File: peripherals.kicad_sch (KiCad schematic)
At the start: 14 parts, among them U5 FT230XQ

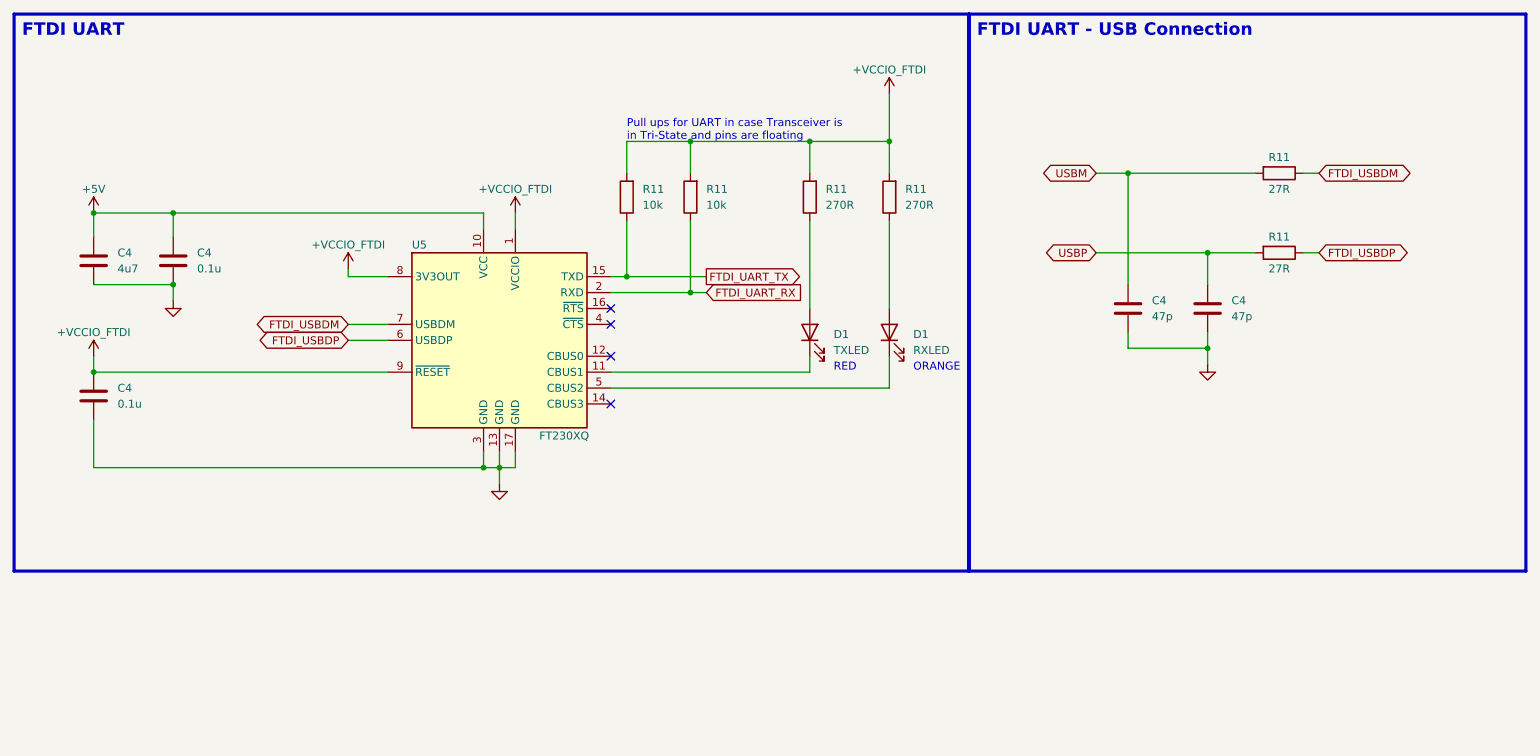
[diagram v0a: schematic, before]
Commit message: Added ESD, updated Footprints, BOM, etc.
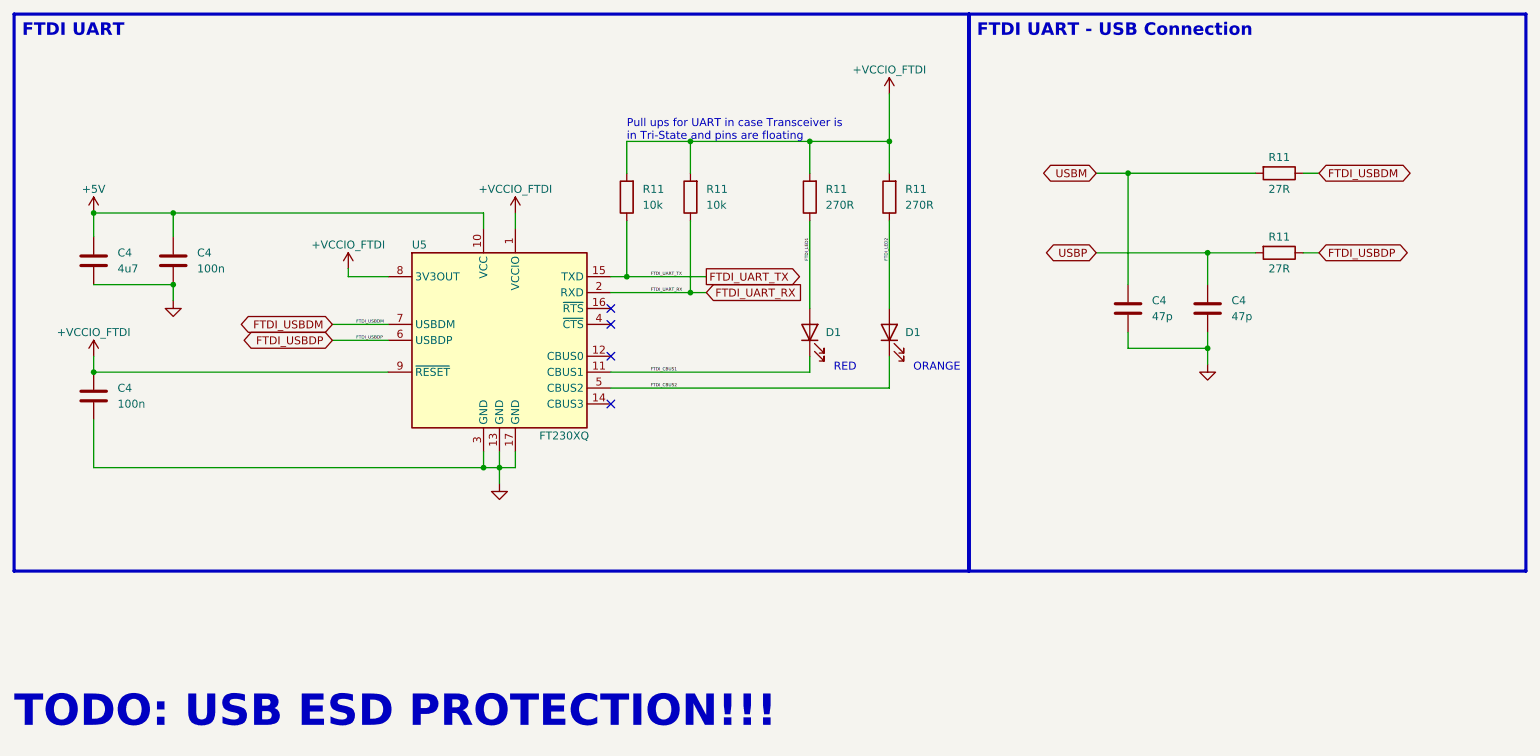
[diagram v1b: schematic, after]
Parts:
- C4: value 0.1u -> 100n
- D1: value TXLED -> SML-LX0402SIC-TR
- D1: value RXLED -> SML-LX0402SOC-TR; Feld4 SML-LX0402SOC-TR -> (none); MFN (none) -> SML-LX0402SOC-TR
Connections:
- net FTDI_CBUS1: now reaches D1.1 (K), U5.11 (CBUS1)
- net FTDI_CBUS2: now reaches D1.1 (K), U5.5 (CBUS2)
- net FTDI_LED2: now reaches D1.2 (A), R11.1
- net FTDI_LED1: now reaches D1.2 (A), R11.1
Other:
- note added: "TODO: USB ESD PROTECTION!!!"
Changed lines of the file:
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@@
     (stroke (width 0) (type default))
   )
-  (wire (pts (xy 78.74 77.47) (xy 85.09 77.47))
+  (wire (pts (xy 76.2 77.47) (xy 85.09 77.47))
     (stroke (width 0) (type default))
   )
@@
     (stroke (width 0) (type default))
   )
-  (wire (pts (xy 78.74 74.93) (xy 85.09 74.93))
+  (wire (pts (xy 76.2 74.93) (xy 85.09 74.93))
     (stroke (width 0) (type default))
   )
@@
     (effects (font (size 2 2) (thickness 0.254) bold (color 100 100 100 1)) (justify left bottom))
   )
+  (text "TODO: USB ESD PROTECTION!!!" (at 25.4 139.7 0)
+    (effects (font (size 5 5) (thickness 1) bold (color 150 0 0 1)) (justify left bottom))
+  )
   (text "Pull ups for UART in case Transceiver is\nin Tri-State and pins are floating"
     (at 123.19 45.72 0)
@@
     (effects (font (size 1.27 1.27)) (justify left bottom))
   )
-  (global_label "FTDI_USBDP" (shape bidirectional) (at 78.74 77.47 180) (fields_autoplaced)
+  (label "FTDI_UART_TX" (at 127 67.31 0) (fields_autoplaced)
+    (effects (font (size 0.5 0.5)) (justify left bottom))
+    (property "Netclass" "UART" (at 127 67.81 0)
+      (effects (font (size 0.5 0.5) italic) (justify left))
+    )
+  )
+  (label "FTDI_USBDP" (at 80.01 77.47 0) (fields_autoplaced)
+    (effects (font (size 0.5 0.5)) (justify left bottom))
+    (property "Netclass" "UART" (at 80.01 77.97 0)
+      (effects (font (size 0.5 0.5) italic) (justify left))
+    )
+  )
+  (label "FTDI_LED1" (at 152.4 64.77 90) (fields_autoplaced)
+    (effects (font (size 0.5 0.5)) (justify left bottom))
+    (property "Netclass" "UART" (at 152.9 64.77 90)
+      (effects (font (size 0.5 0.5) italic) (justify left))
+    )
+  )
+  (label "FTDI_UART_RX" (at 127 69.85 0) (fields_autoplaced)
+    (effects (font (size 0.5 0.5)) (justify left bottom))
+    (property "Netclass" "UART" (at 127 70.35 0)
+      (effects (font (size 0.5 0.5) italic) (justify left))
+    )
+  )
+  (label "FTDI_CBUS2" (at 127 85.09 0) (fields_autoplaced)
+    (effects (font (size 0.5 0.5)) (justify left bottom))
+    (property "Netclass" "UART" (at 127 85.59 0)
+      (effects (font (size 0.5 0.5) italic) (justify left))
+    )
+  )
+  (label "FTDI_CBUS1" (at 127 82.55 0) (fields_autoplaced)
+    (effects (font (size 0.5 0.5)) (justify left bottom))
+    (property "Netclass" "UART" (at 127 83.05 0)
+      (effects (font (size 0.5 0.5) italic) (justify left))
+    )
+  )
+  (label "FTDI_USBDM" (at 80.01 74.93 0) (fields_autoplaced)
+    (effects (font (size 0.5 0.5)) (justify left bottom))
+    (property "Netclass" "UART" (at 80.01 75.43 0)
+      (effects (font (size 0.5 0.5) italic) (justify left))
+    )
+  )
+  (label "FTDI_LED2" (at 165.1 64.77 90) (fields_autoplaced)
+    (effects (font (size 0.5 0.5)) (justify left bottom))
+    (property "Netclass" "UART" (at 165.6 64.77 90)
+      (effects (font (size 0.5 0.5) italic) (justify left))
+    )
+  )
+  (global_label "FTDI_USBDP" (shape bidirectional) (at 76.2 77.47 180) (fields_autoplaced)
     (effects (font (size 1.27 1.27)) (justify right))
-    (property "Intersheetrefs" "${INTERSHEET_REFS}" (at 63.3949 77.47 0)
+    (property "Intersheetrefs" "${INTERSHEET_REFS}" (at 60.8549 77.47 0)
       (effects (font (size 1.27 1.27)) (justify right) hide)
     )
@@
     )
   )
-  (global_label "FTDI_USBDM" (shape bidirectional) (at 78.74 74.93 180) (fields_autoplaced)
+  (global_label "FTDI_USBDM" (shape bidirectional) (at 76.2 74.93 180) (fields_autoplaced)
     (effects (font (size 1.27 1.27)) (justify right))
-    (property "Intersheetrefs" "${INTERSHEET_REFS}" (at 63.2135 74.93 0)
+    (property "Intersheetrefs" "${INTERSHEET_REFS}" (at 60.6735 74.93 0)
       (effects (font (size 1.27 1.27)) (justify right) hide)
     )
@@
       (effects (font (size 1.27 1.27)) (justify left))
     )
-    (property "Value" "0.1u" (at 41.91 87.63 0)
+    (property "Value" "100n" (at 41.91 87.63 0)
       (effects (font (size 1.27 1.27)) (justify left))
     )
@@
       (effects (font (size 1.27 1.27)) hide)
     )
-    (property "Datasheet" "https://www.mouser.de/datasheet/2/40/AutoMLCCKAM-3216307.pdf" (at 38.1 86.36 0)
+    (property "Datasheet" "~" (at 38.1 86.36 0)
       (effects (font (size 1.27 1.27)) hide)
     )
@@
       (effects (font (size 1.27 1.27)) hide)
     )
-    (property "Datasheet" "https://www.mouser.de/datasheet/2/40/AutoMLCCKAM-3216307.pdf" (at 203.2 72.39 0)
+    (property "Datasheet" "~" (at 203.2 72.39 0)
       (effects (font (size 1.27 1.27)) hide)
     )
@@
   )
   (symbol (lib_id "Device:LED") (at 152.4 76.2 90) (unit 1)
-    (in_bom yes) (on_board yes) (dnp no) (fields_autoplaced)
-    (property "Reference" "D1" (at 156.21 76.5175 90)
-      (effects (font (size 1.27 1.27)) (justify right))
-    )
-    (property "Value" "TXLED" (at 156.21 79.0575 90)
-      (effects (font (size 1.27 1.27)) (justify right))
+    (in_bom yes) (on_board yes) (dnp no)
+    (property "Reference" "D1" (at 154.94 76.2 90)
+      (effects (font (size 1.27 1.27)) (justify right))
+    )
+    (property "Value" "SML-LX0402SIC-TR" (at 142.24 73.66 90)
+      (effects (font (size 1.27 1.27)) (justify right) hide)
     )
     (property "Footprint" "LED_SMD:LED_0402_1005Metric" (at 152.4 76.2 0)
       (effects (font (size 1.27 1.27)) hide)
     )
-    (property "Datasheet" "https://www.mouser.de/datasheet/2/244/LUMXS09183_1-2551481.pdf" (at 152.4 76.2 0)
+    (property "Datasheet" "~" (at 152.4 76.2 0)
       (effects (font (size 1.27 1.27)) hide)
     )
@@
       (effects (font (size 1.27 1.27)) hide)
     )
-    (property "Datasheet" "https://www.mouser.de/datasheet/2/40/AutoMLCCKAM-3216307.pdf" (at 215.9 72.39 0)
+    (property "Datasheet" "~" (at 215.9 72.39 0)
       (effects (font (size 1.27 1.27)) hide)
     )
@@
       (effects (font (size 1.27 1.27)) hide)
     )
-    (property "Datasheet" "https://www.mouser.de/datasheet/2/40/AutoMLCCKAM-3216307.pdf" (at 38.1 64.77 0)
+    (property "Datasheet" "~" (at 38.1 64.77 0)
       (effects (font (size 1.27 1.27)) hide)
     )
@@
   )
   (symbol (lib_id "Device:LED") (at 165.1 76.2 90) (unit 1)
-    (in_bom yes) (on_board yes) (dnp no) (fields_autoplaced)
-    (property "Reference" "D1" (at 168.91 76.5175 90)
-      (effects (font (size 1.27 1.27)) (justify right))
-    )
-    (property "Value" "RXLED" (at 168.91 79.0575 90)
-      (effects (font (size 1.27 1.27)) (justify right))
+    (in_bom yes) (on_board yes) (dnp no)
+    (property "Reference" "D1" (at 167.64 76.2 90)
+      (effects (font (size 1.27 1.27)) (justify right))
+    )
+    (property "Value" "SML-LX0402SOC-TR" (at 156.21 73.66 90)
+      (effects (font (size 1.27 1.27)) (justify right) hide)
     )
     (property "Footprint" "LED_SMD:LED_0402_1005Metric" (at 165.1 76.2 0)
       (effects (font (size 1.27 1.27)) hide)
     )
-    (property "Datasheet" "https://www.mouser.de/datasheet/2/244/LUMXS09145_1-2551480.pdf" (at 165.1 76.2 0)
-      (effects (font (size 1.27 1.27)) hide)
-    )
-    (property "Feld4" "SML-LX0402SOC-TR" (at 165.1 76.2 90)
+    (property "Datasheet" "~" (at 165.1 76.2 0)
+      (effects (font (size 1.27 1.27)) hide)
+    )
+    (property "MFN" "SML-LX0402SOC-TR" (at 165.1 76.2 90)
       (effects (font (size 1.27 1.27)) hide)
     )
@@
       (effects (font (size 1.27 1.27)) (justify left))
     )
-    (property "Value" "0.1u" (at 54.61 66.04 0)
+    (property "Value" "100n" (at 54.61 66.04 0)
       (effects (font (size 1.27 1.27)) (justify left))
     )
@@
       (effects (font (size 1.27 1.27)) hide)
     )
-    (property "Datasheet" "https://www.mouser.de/datasheet/2/40/AutoMLCCKAM-3216307.pdf" (at 50.8 64.77 0)
-      (effects (font (size 1.27 1.27)) hide)
-    )
+    (property "Datasheet" "~" (at 50.8 64.77 0)
+      (effects (font (size 1.27 1.27)) hide)
+    )
